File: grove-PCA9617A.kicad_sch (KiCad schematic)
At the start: 5 parts, among them J1 Grove-I2C-connector, J2 Grove-I2C-connector, U1 PCA9617

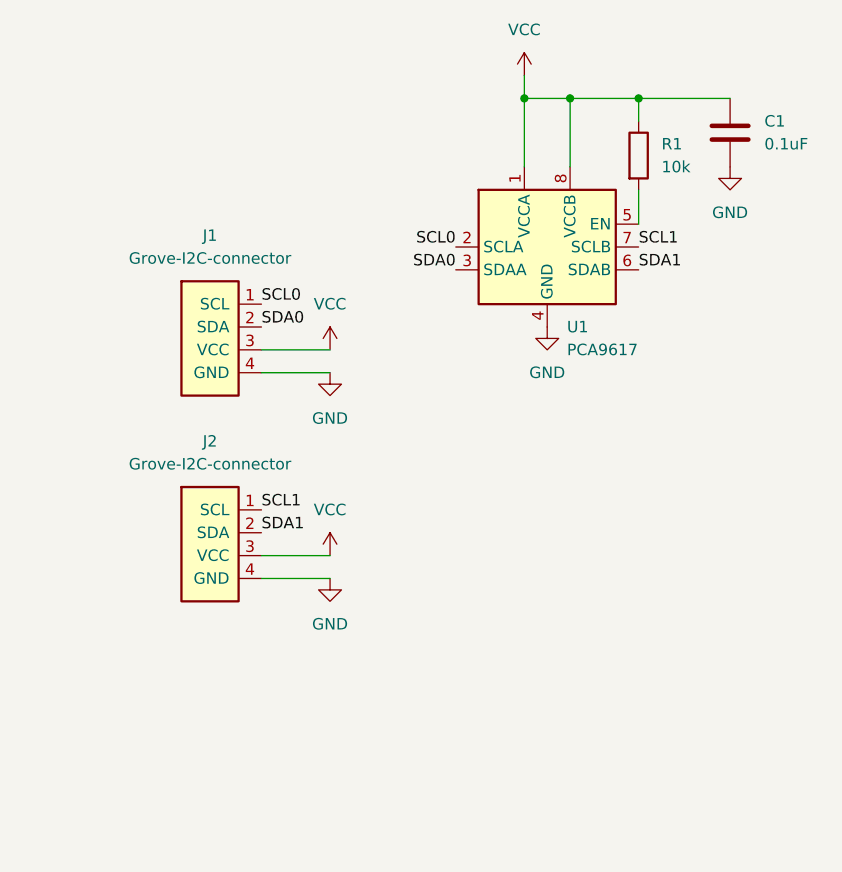
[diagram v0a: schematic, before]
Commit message: Add pullup resistors
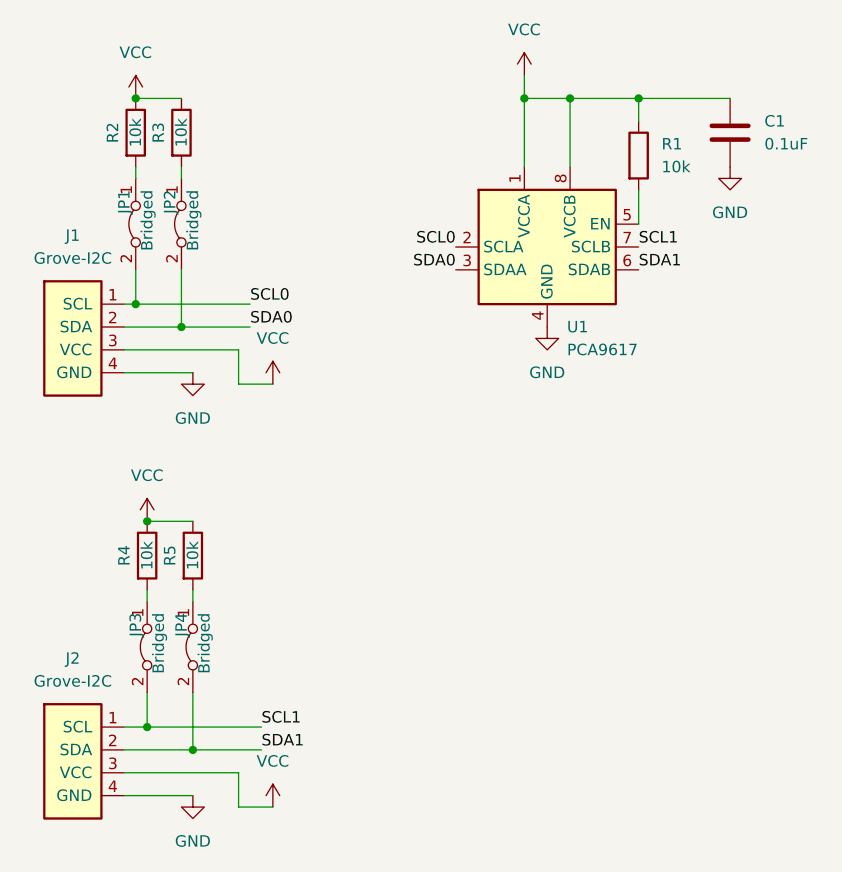
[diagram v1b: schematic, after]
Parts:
- added JP1, JP2, JP3, JP4: Bridged, Jumper:SolderJumper-2_P1.3mm_Bridged_RoundedPad1.0x1.5mm, symbol Jumper:Jumper_2_Bridged
- added R2, R3, R4, R5: 10k, Resistor_SMD:R_0402_1005Metric, symbol Device:R
- J1, J2: value Grove-I2C-connector -> Grove-I2C
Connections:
- net SCL0: now also JP1.2 (B)
- net SCL1: now also JP3.2 (B)
- net SDA0: now also JP2.2 (B)
- net SDA1: now also JP4.2 (B)
- net VCC: now also R2.1, R3.1, R4.1, R5.1
- new net: JP3.1 (A), R4.2
- new net: JP2.1 (A), R3.2
- new net: JP1.1 (A), R2.2
- new net: JP4.1 (A), R5.2
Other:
- moved on the sheet: J1, J2
